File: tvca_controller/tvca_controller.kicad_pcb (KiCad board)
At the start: 2 copper layers, 44 parts, among them J1 Programming Header, J2 CAN connector, J3 Batt, J4 Screw_Terminal_01x04, J5 4DB-P108-02, J6 Screw_Terminal_01x04, J7 4DB-P108-02, J8 Batt, U1 PIC18F26K83, U2 MCP2562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

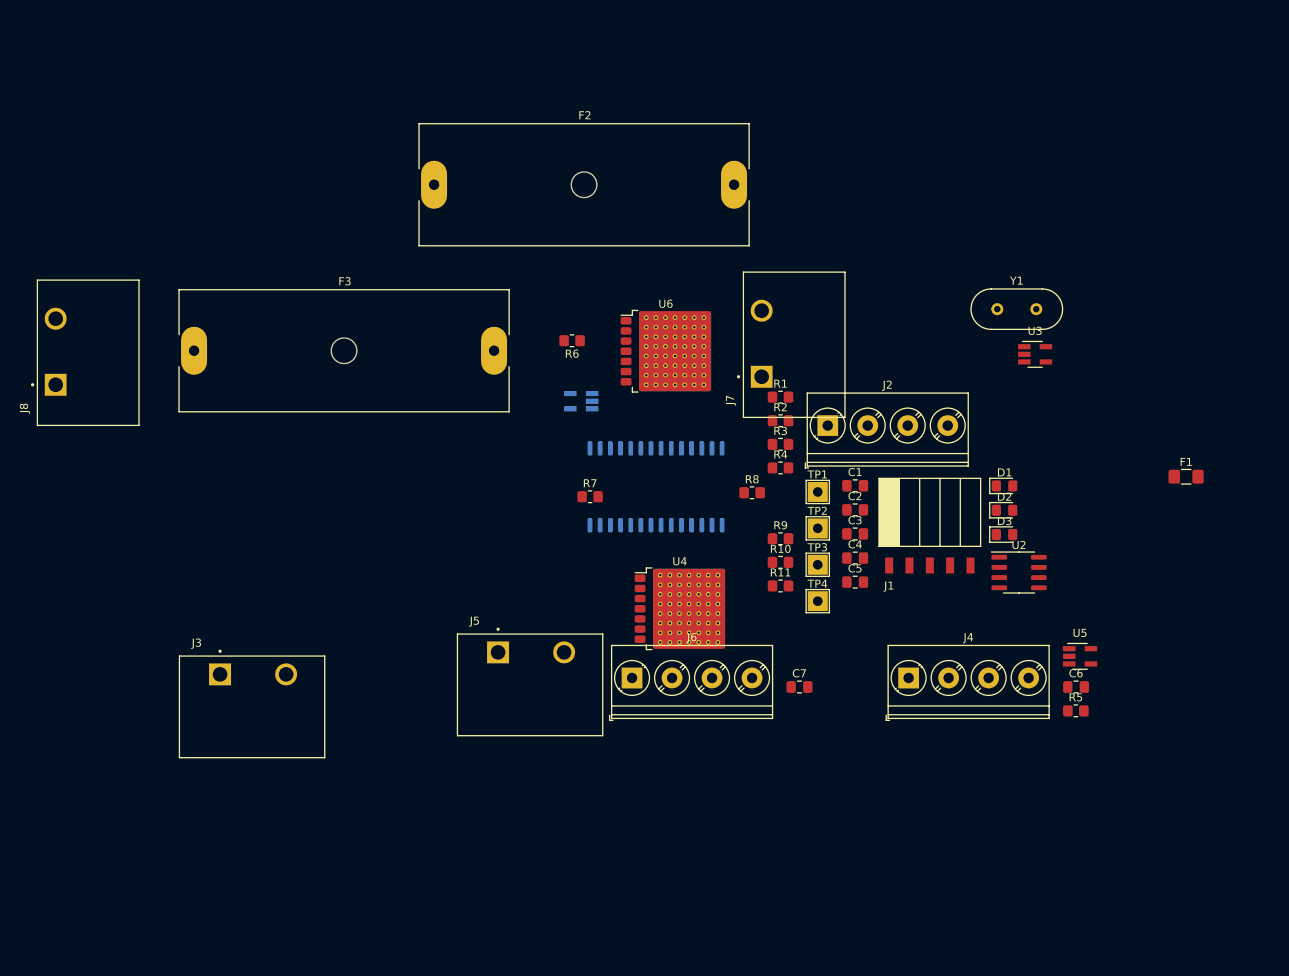
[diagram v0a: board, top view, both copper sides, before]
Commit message: Replace motor controller IC
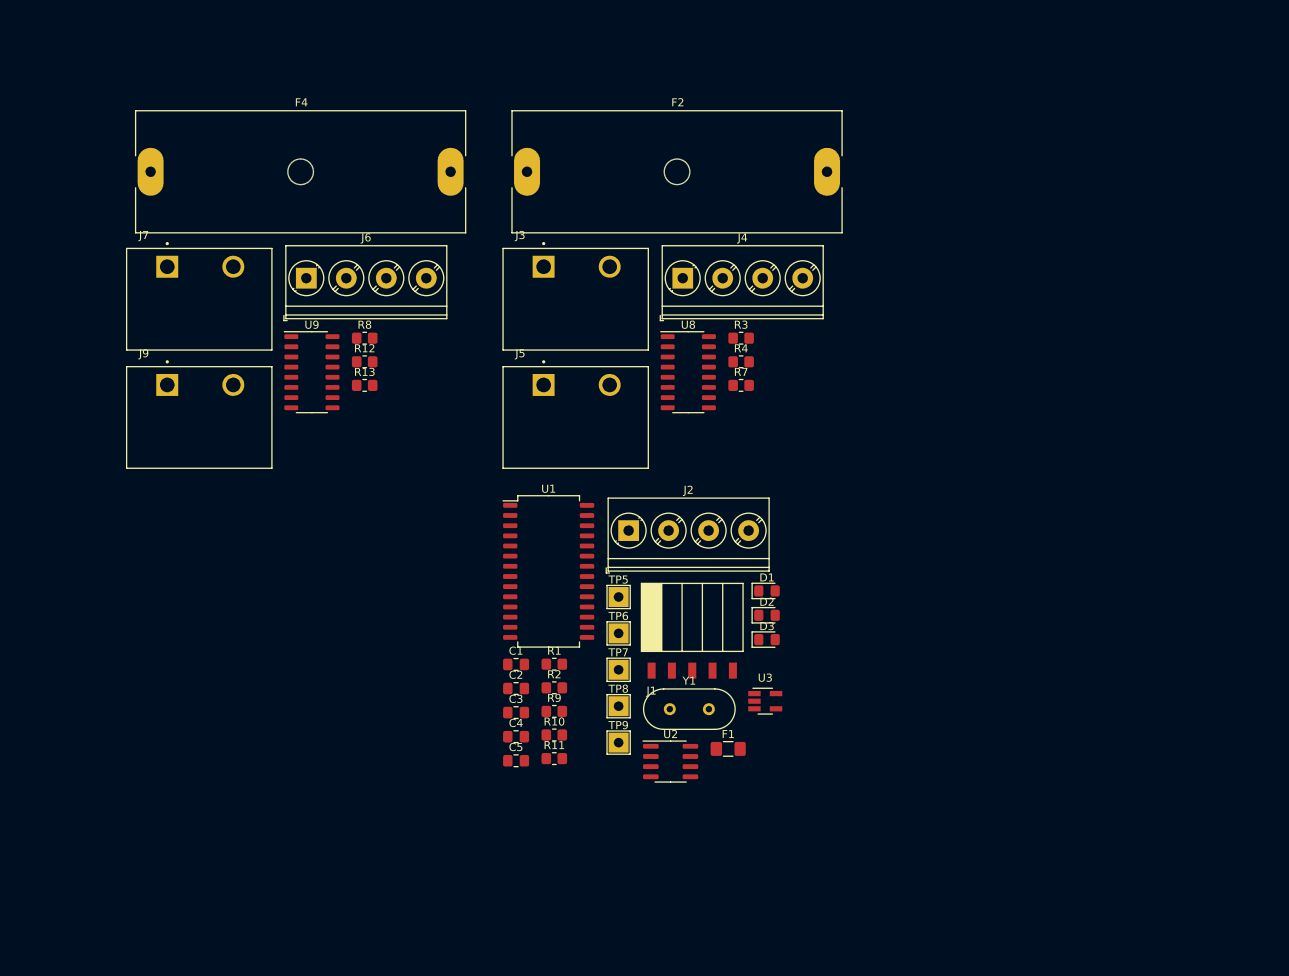
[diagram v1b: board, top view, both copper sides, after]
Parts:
- removed C6, C7: 0.1 uF, Capacitor_SMD:C_0805_2012Metric_Pad1.18x1.45mm_HandSolder
- removed F3: 25 A, Fuse:Fuseholder_Cylinder-6.3x32mm_Schurter_0031-8002_Horizontal_Open
- removed J8: Batt, canhw_footprints:TE_2-1437667-4
- removed R5, R6: 2 mR, Resistor_SMD:R_0805_2012Metric_Pad1.20x1.40mm_HandSolder
- removed TP1: RIN_1, TestPoint:TestPoint_THTPad_2.5x2.5mm_Drill1.2mm
- removed TP2: FIN_1, TestPoint:TestPoint_THTPad_2.5x2.5mm_Drill1.2mm
- removed TP3: RIN_2, TestPoint:TestPoint_THTPad_2.5x2.5mm_Drill1.2mm
- removed TP4: FIN_2, TestPoint:TestPoint_THTPad_2.5x2.5mm_Drill1.2mm
- removed U4, U6: BD6222HFP, Package_TO_SOT_SMD:Rohm_HRP7
- removed U5, U7: INA180, Package_TO_SOT_SMD:SOT-23-5_HandSoldering
- added F4: 25 A, Fuse:Fuseholder_Cylinder-6.3x32mm_Schurter_0031-8002_Horizontal_Open, F.Cu at (63.6, 61.9)
- added J9: 4DB-P108-02, canhw_footprints:TE_2-1437667-4, F.Cu at (65.7, 88.5)
- added R12: 21.5k 1%, Resistor_SMD:R_0805_2012Metric_Pad1.20x1.40mm_HandSolder, F.Cu at (90.3, 85.6)
- added R13: 10k 1%, Resistor_SMD:R_0805_2012Metric_Pad1.20x1.40mm_HandSolder, F.Cu at (90.3, 88.6)
- added TP5: 5V, TestPoint:TestPoint_THTPad_2.5x2.5mm_Drill1.2mm, F.Cu at (122.1, 115.0)
- added TP6: GND, TestPoint:TestPoint_THTPad_2.5x2.5mm_Drill1.2mm, F.Cu at (122.1, 119.6)
- added TP7: CANH, TestPoint:TestPoint_THTPad_2.5x2.5mm_Drill1.2mm, F.Cu at (122.1, 124.1)
- added TP8: CANL, TestPoint:TestPoint_THTPad_2.5x2.5mm_Drill1.2mm, F.Cu at (122.1, 128.7)
- added TP9: 5V current draw, TestPoint:TestPoint_THTPad_2.5x2.5mm_Drill1.2mm, F.Cu at (122.1, 133.2)
- added U8: ~, Package_SO:SO-16_3.9x9.9mm_P1.27mm, F.Cu at (130.8, 86.9)
- added U9: ~, Package_SO:SO-16_3.9x9.9mm_P1.27mm, F.Cu at (83.7, 86.9)
- J2: value CAN connector -> PT 1,5/ 4-5,0-H
- J3: value Batt -> 4DB-P108-02
- J4, J6: value Screw_Terminal_01x04 -> PT 1,5/ 4-5,0-H
- R1: value 10 kR -> 10 K
- R2: value 200 mR -> 200 mR 1%
- R7: value 21.5k 1% -> R_SENSE
- R8: value 10k 1% -> R_SENSE
- U1: moved to F.Cu
- Y1: value Crystal -> Crystal 12 MHz
- moved J7 75.6 mm to (65.7, 73.7), turned to 0 degrees
- moved F1 66.6 mm to (135.8, 134.0)
- moved J3 65.1 mm to (112.7, 73.7)
- moved Y1 64.6 mm to (128.5, 129.1)
- moved J6 64.5 mm to (83.0, 75.2)
- moved J4 57.4 mm to (130.1, 75.2)
- moved U3 54.9 mm to (140.4, 128.1)
- moved R8 52.1 mm to (90.3, 82.7)
- moved U2 49.5 mm to (128.6, 135.6)
- moved C4 47.9 mm to (109.2, 132.5)
- moved C1 47.9 mm to (109.2, 123.5)
- moved C2 47.9 mm to (109.2, 126.5)
- moved C5 47.9 mm to (109.2, 135.5)
- moved C3 47.9 mm to (109.2, 129.5)
- moved R1 43.7 mm to (114.0, 123.4)
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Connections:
- net /BATT_1 renamed /Motor_1/BATT
- F1 pad 1: Net-(J2-Pin_1) -> Net-(J2-Pin_2)
- J2 pad 1: Net-(J2-Pin_1) -> GND
- J2 pad 2: GND -> Net-(J2-Pin_2)
- R10 pad 1: Net-(U1-RC6) -> Net-(U1-RB4)
- R11 pad 1: Net-(U1-RC5) -> Net-(U1-RB3)
- R3 pad 2: /VBAT -> /VBAT_1
- R4 pad 1: /VBAT -> /VBAT_1
- R7 pad 1: /BATT_2 -> /CUR_1
- R7 pad 2: /VBAT -> Net-(U8-CS)
- R8 pad 1: /VBAT -> /CUR_2
- R8 pad 2: GND -> Net-(U9-CS)
- R9 pad 1: Net-(U1-RC7) -> Net-(U1-RB5)
- U1 pad 13: /VBAT -> /IN_B_1
- U1 pad 14: /CUR_1 -> /IN_A_1
- U1 pad 15: /CUR_2 -> /PWM_1
- U1 pad 16: Net-(U1-RC5) -> /PWM_2
- U1 pad 17: Net-(U1-RC6) -> /IN_A_2
- U1 pad 18: Net-(U1-RC7) -> /CUR_2
- U1 pad 21: /FIN_1 -> /CUR_1
- U1 pad 22: /RIN_1 -> /VBAT_2
- U1 pad 23: unconnected-(U1-RB2-Pad23) -> /VBAT_1
- U1 pad 24: unconnected-(U1-RB3-Pad24) -> Net-(U1-RB3)
- U1 pad 25: /RIN_2 -> Net-(U1-RB4)
- U1 pad 26: /FIN_2 -> Net-(U1-RB5)
- U1 pad 7: unconnected-(U1-RA5-Pad7) -> /IN_B_2

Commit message: Update motor controller IC and fuse holders
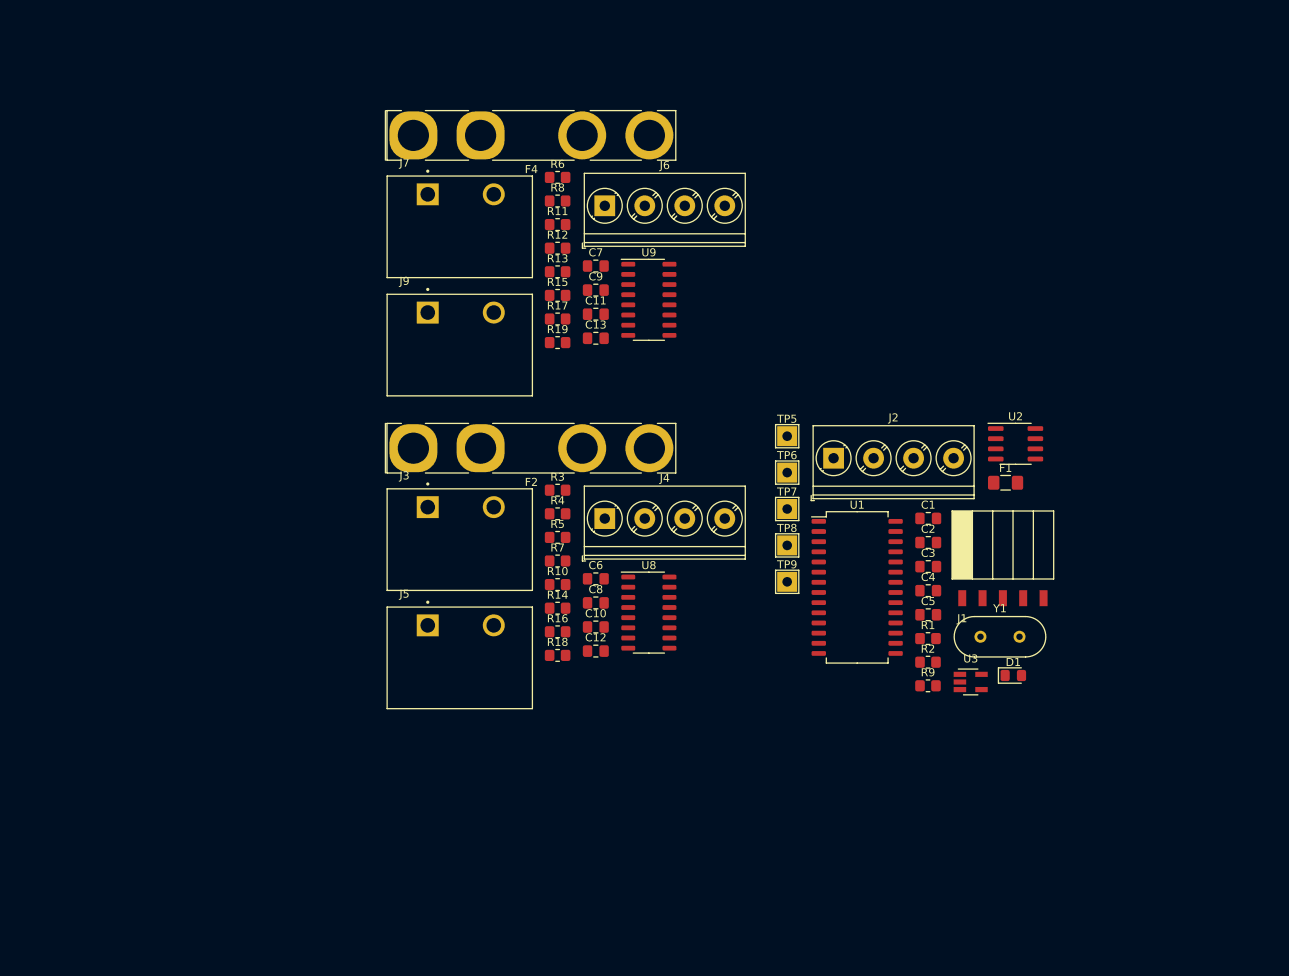
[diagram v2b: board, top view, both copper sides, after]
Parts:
- removed D2: BLUE, LED_SMD:LED_0805_2012Metric_Pad1.15x1.40mm_HandSolder
- removed D3: GREEN, LED_SMD:LED_0805_2012Metric_Pad1.15x1.40mm_HandSolder
- added C10: 270 uF, Capacitor_SMD:C_0805_2012Metric_Pad1.18x1.45mm_HandSolder, F.Cu at (119.2, 118.8)
- added C11: 270 uF, Capacitor_SMD:C_0805_2012Metric_Pad1.18x1.45mm_HandSolder, F.Cu at (119.2, 79.7)
- added C12: 0.1 uF, Capacitor_SMD:C_0805_2012Metric_Pad1.18x1.45mm_HandSolder, F.Cu at (119.2, 121.8)
- added C13: 0.1 uF, Capacitor_SMD:C_0805_2012Metric_Pad1.18x1.45mm_HandSolder, F.Cu at (119.2, 82.7)
- added C6: 10 nF, Capacitor_SMD:C_0805_2012Metric_Pad1.18x1.45mm_HandSolder, F.Cu at (119.2, 112.8)
- added C7: 10 nF, Capacitor_SMD:C_0805_2012Metric_Pad1.18x1.45mm_HandSolder, F.Cu at (119.2, 73.7)
- added C8: 100 nF, Capacitor_SMD:C_0805_2012Metric_Pad1.18x1.45mm_HandSolder, F.Cu at (119.2, 115.8)
- added C9: 100 nF, Capacitor_SMD:C_0805_2012Metric_Pad1.18x1.45mm_HandSolder, F.Cu at (119.2, 76.7)
- added R14: 1 K, Resistor_SMD:R_0805_2012Metric_Pad1.20x1.40mm_HandSolder, F.Cu at (114.4, 116.4)
- added R15: 1 K, Resistor_SMD:R_0805_2012Metric_Pad1.20x1.40mm_HandSolder, F.Cu at (114.4, 77.3)
- added R16: 1 K, Resistor_SMD:R_0805_2012Metric_Pad1.20x1.40mm_HandSolder, F.Cu at (114.4, 119.4)
- added R17: 1 K, Resistor_SMD:R_0805_2012Metric_Pad1.20x1.40mm_HandSolder, F.Cu at (114.4, 80.3)
- added R18: 10 K, Resistor_SMD:R_0805_2012Metric_Pad1.20x1.40mm_HandSolder, F.Cu at (114.4, 122.3)
- added R19: 10 K, Resistor_SMD:R_0805_2012Metric_Pad1.20x1.40mm_HandSolder, F.Cu at (114.4, 83.2)
- added R5: 1 K, Resistor_SMD:R_0805_2012Metric_Pad1.20x1.40mm_HandSolder, F.Cu at (114.4, 107.6)
- added R6: 1 K, Resistor_SMD:R_0805_2012Metric_Pad1.20x1.40mm_HandSolder, F.Cu at (114.4, 62.6)
- F2, F4: footprint Fuse:Fuseholder_Cylinder-6.3x32mm_Schurter_0031-8002_Horizontal_Open -> Fuse:Fuseholder_Keystone_3555-2
- R10, R11: value 330 R -> 1 K
- U8, U9: value ~ -> VNH7070AS
- moved R11 66.8 mm to (114.4, 68.5)
- moved U2 58.6 mm to (171.7, 95.9)
- moved C4 54.7 mm to (160.8, 114.2)
- moved C1 54.7 mm to (160.8, 105.2)
- moved C2 54.7 mm to (160.8, 108.2)
- moved C3 54.7 mm to (160.8, 111.2)
- moved C5 54.7 mm to (160.8, 117.2)
- moved F1 48.1 mm to (170.4, 100.8)
- moved R9 46.8 mm to (160.7, 126.1)
- moved R1 46.8 mm to (160.7, 120.2)
- moved R2 46.8 mm to (160.7, 123.2)
- moved U9 43.1 mm to (125.8, 77.9)
- moved Y1 39.9 mm to (167.3, 120.0)
- moved J1 39.9 mm to (165.0, 115.2)
- moved U1 38.6 mm to (151.9, 113.8)
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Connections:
- net /A_1 renamed /ENCDRA_1
- net /A_2 renamed /ENCDRA_2
- net /B_1 renamed /ENCDRB_1
- net /B_2 renamed /ENCDRB_2
- F2 pad 2: /Motor_1/BATT -> /Motor_1/POWER
- F4 pad 2: /Motor_2/BATT -> /Motor_2/POWER
- R10 pad 1: Net-(U1-RB4) -> Net-(U8-IN_B)
- R10 pad 2: Net-(D2-K) -> /CCW_1
- R11 pad 1: Net-(U1-RB3) -> Net-(U9-IN_B)
- R11 pad 2: Net-(D3-K) -> /CCW_2
- R12 pad 1: /Motor_2/BATT -> /Motor_2/POWER
- R3 pad 1: /Motor_1/BATT -> /Motor_1/POWER
- R7 pad 1: /CUR_1 -> Net-(U8-CS)
- R7 pad 2: Net-(U8-CS) -> GND
- R8 pad 1: /CUR_2 -> Net-(U9-CS)
- R8 pad 2: Net-(U9-CS) -> GND
- U1 pad 13: /IN_B_1 -> /CCW_1
- U1 pad 14: /IN_A_1 -> /CLW_1
- U1 pad 17: /IN_A_2 -> /CLW_2
- U1 pad 24: Net-(U1-RB3) -> /SEL_2
- U1 pad 25: Net-(U1-RB4) -> /SEL_1
- U1 pad 7: /IN_B_2 -> /CCW_2
- U8 pad 11: /PWM_1 -> Net-(U8-PWM)
- U8 pad 14: +5V -> Net-(U8-SEL_0)
- U8 pad 3: /IN_A_1 -> Net-(U8-IN_A)
- U8 pad 6: /IN_B_1 -> Net-(U8-IN_B)
- U9 pad 11: /PWM_2 -> Net-(U9-PWM)
- U9 pad 14: +5V -> Net-(U9-SEL_0)
- U9 pad 3: /IN_A_2 -> Net-(U9-IN_A)
- U9 pad 6: /IN_B_2 -> Net-(U9-IN_B)

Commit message: changes
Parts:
- moved J1 61.1 mm to (176.7, 55.2)
- moved Y1 58.4 mm to (155.8, 62.8)
- moved U1 55.3 mm to (178.2, 65.2), turned to 90 degrees
- moved U2 53.7 mm to (194.5, 47.2)
- moved F1 53.5 mm to (195.0, 53.2)
- moved J2 49.5 mm to (154.2, 48.5)
- moved TP5 30.9 mm to (174.0, 93.3)
- moved TP6 30.9 mm to (174.0, 97.9)
- moved TP7 30.9 mm to (174.0, 102.5)
- moved TP8 30.9 mm to (174.0, 107.0)
- moved TP9 30.9 mm to (174.0, 111.5)
- moved R2 30.9 mm to (191.6, 121.6)
- moved U3 30.9 mm to (196.9, 124.1)
- moved C1 30.9 mm to (191.6, 103.6)
- moved C2 30.9 mm to (191.6, 106.6)
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
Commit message: new footprint
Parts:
- C10, C11: footprint Capacitor_SMD:C_0805_2012Metric_Pad1.18x1.45mm_HandSolder -> Capacitor_THT:CP_Radial_D12.5mm_P5.00mm
- D1: footprint LED_SMD:LED_0805_2012Metric_Pad1.15x1.40mm_HandSolder -> LED_SMD:LED_1206_3216Metric_Pad1.42x1.75mm_HandSolder
- F2, F4: footprint Fuse:Fuseholder_Keystone_3555-2 -> canhw_footprints:Fuseholder_36-3557-15-ND
- moved F1 93.8 mm to (165.4, 142.3)
- moved J1 78.2 mm to (164.3, 132.5)
- moved Y1 75.3 mm to (166.6, 137.3)
- moved F2 75.1 mm to (168.6, 75.7)
- moved U1 71.2 mm to (151.2, 131.2), turned to 0 degrees
- moved U2 70.0 mm to (171.0, 113.2)
- moved U8 69.2 mm to (176.7, 70.1)
- moved C12 67.7 mm to (174.9, 83.3)
- moved J2 66.8 mm to (148.2, 115.0)
- moved C6 66.0 mm to (174.9, 77.3)
- moved C8 66.0 mm to (174.9, 80.3)
- moved J3 59.7 mm to (146.0, 68.0)
- moved J5 59.7 mm to (146.0, 82.7)
- moved R14 59.7 mm to (162.2, 80.6)
- moved R3 59.7 mm to (162.2, 65.8)
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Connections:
- F1 pad 1: Net-(J2-Pin_2) -> Net-(J2-Pin_1)
- J2 pad 1: GND -> Net-(J2-Pin_1)
- J2 pad 2: Net-(J2-Pin_2) -> /CANH
- J2 pad 3: /CANH -> /CANL
- J2 pad 4: /CANL -> GND
